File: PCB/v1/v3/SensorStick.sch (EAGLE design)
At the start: 56 parts, among them U1 TPD4F003DQDR, Y1 ECS-TXO-3225MV-400-TR

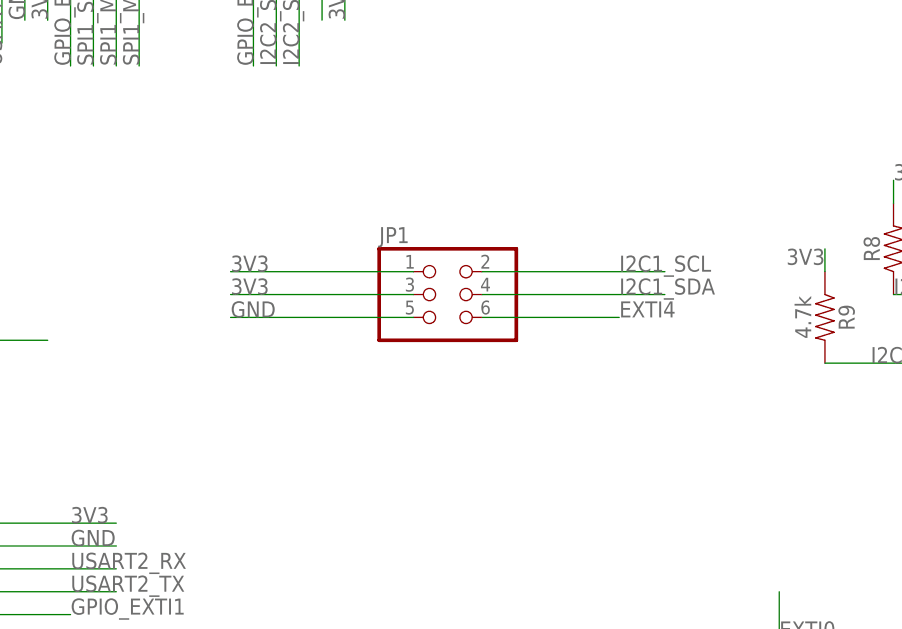
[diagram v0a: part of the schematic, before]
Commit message: Jesus - Rearranged to fit DIL24 socket for Mag breakout
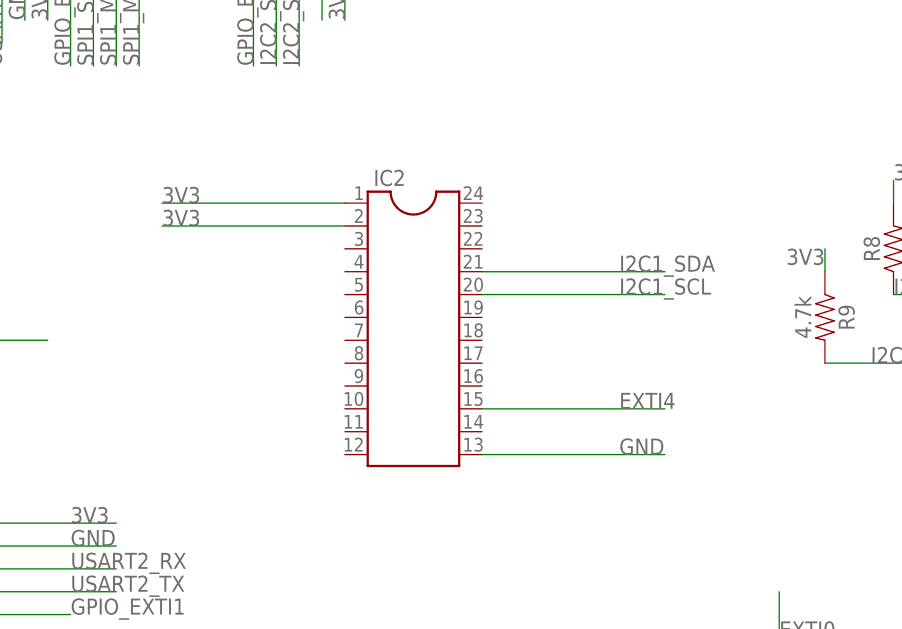
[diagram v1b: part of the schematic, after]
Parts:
- removed JP1: (no value), pinhead:PINHD-2X3
- added IC2: (no value), ic-package:DIL24-6
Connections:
- net 3V3: now also IC2.1, IC2.2; no longer JP1.1, JP1.3
- net EXTI4: now also IC2.15; no longer JP1.6
- net GND: now also IC2.13; no longer JP1.5
- net I2C1_SCL: now also IC2.20; no longer JP1.2
- net I2C1_SDA: now also IC2.21; no longer JP1.4
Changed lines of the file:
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@@
 <part name="U1" library="TPD4F003DQDR" deviceset="TPD4F003DQDR" device=""/>
 <part name="SV1" library="con-lsta" library_urn="urn:adsk.eagle:library:161" deviceset="FE05-1" device="" package3d_urn="urn:adsk.eagle:package:8190/1"/>
-<part name="JP1" library="pinhead" library_urn="urn:adsk.eagle:library:325" deviceset="PINHD-2X3" device="" package3d_urn="urn:adsk.eagle:package:22462/2"/>
 <part name="FRAME1" library="frames" library_urn="urn:adsk.eagle:library:229" deviceset="DINA3_L" device=""/>
+<part name="IC2" library="ic-package" library_urn="urn:adsk.eagle:library:239" deviceset="DIL24" device="-6" package3d_urn="urn:adsk.eagle:package:1009/2"/>
 </parts>
 <sheets>
@@
 <attribute name="NAME" x="102.87" y="97.282" size="1.778" layer="95"/>
 </instance>
-<instance part="JP1" gate="A" x="165.1" y="119.38" smashed="yes">
-<attribute name="NAME" x="158.75" y="125.095" size="1.778" layer="95"/>
-<attribute name="VALUE" x="158.75" y="111.76" size="1.778" layer="96"/>
-</instance>
 <instance part="FRAME1" gate="G$1" x="0" y="0" smashed="yes"/>
 <instance part="FRAME1" gate="G$2" x="287.02" y="0" smashed="yes">
@@
 <attribute name="SHEET" x="373.38" y="1.27" size="2.54" layer="94"/>
 <attribute name="DRAWING_NAME" x="304.8" y="19.05" size="2.54" layer="94"/>
+</instance>
+<instance part="IC2" gate="G$1" x="162.56" y="114.3" smashed="yes">
+<attribute name="NAME" x="158.115" y="131.445" size="1.778" layer="95"/>
+<attribute name="VALUE" x="158.115" y="97.79" size="1.778" layer="96"/>
 </instance>
 </instances>
@@
 </segment>
 <segment>
-<wire x1="162.56" y1="119.38" x2="142.24" y2="119.38" width="0.1524" layer="91"/>
-<label x="142.24" y="119.38" size="1.778" layer="95"/>
-<pinref part="JP1" gate="A" pin="3"/>
-</segment>
-<segment>
-<wire x1="162.56" y1="121.92" x2="142.24" y2="121.92" width="0.1524" layer="91"/>
-<pinref part="JP1" gate="A" pin="1"/>
-<label x="142.24" y="121.92" size="1.778" layer="95"/>
+<wire x1="154.94" y1="127" x2="134.62" y2="127" width="0.1524" layer="91"/>
+<label x="134.62" y="127" size="1.778" layer="95"/>
+<pinref part="IC2" gate="G$1" pin="2"/>
+</segment>
+<segment>
+<wire x1="154.94" y1="129.54" x2="134.62" y2="129.54" width="0.1524" layer="91"/>
+<label x="134.62" y="129.54" size="1.778" layer="95"/>
+<pinref part="IC2" gate="G$1" pin="1"/>
 </segment>
 </net>
@@
 </segment>
 <segment>
-<wire x1="162.56" y1="116.84" x2="142.24" y2="116.84" width="0.1524" layer="91"/>
-<label x="142.24" y="116.84" size="1.778" layer="95"/>
-<pinref part="JP1" gate="A" pin="5"/>
+<wire x1="170.18" y1="101.6" x2="190.5" y2="101.6" width="0.1524" layer="91"/>
+<label x="185.42" y="101.6" size="1.778" layer="95"/>
+<pinref part="IC2" gate="G$1" pin="13"/>
 </segment>
 </net>
@@
 </segment>
 <segment>
-<wire x1="190.5" y1="119.38" x2="170.18" y2="119.38" width="0.1524" layer="91"/>
-<label x="185.42" y="119.38" size="1.778" layer="95"/>
-<pinref part="JP1" gate="A" pin="4"/>
+<wire x1="190.5" y1="121.92" x2="170.18" y2="121.92" width="0.1524" layer="91"/>
+<label x="185.42" y="121.92" size="1.778" layer="95"/>
+<pinref part="IC2" gate="G$1" pin="21"/>
 </segment>
 </net>
@@
 </segment>
 <segment>
-<wire x1="190.5" y1="121.92" x2="170.18" y2="121.92" width="0.1524" layer="91"/>
-<label x="185.42" y="121.92" size="1.778" layer="95"/>
-<pinref part="JP1" gate="A" pin="2"/>
+<wire x1="190.5" y1="119.38" x2="170.18" y2="119.38" width="0.1524" layer="91"/>
+<label x="185.42" y="119.38" size="1.778" layer="95"/>
+<pinref part="IC2" gate="G$1" pin="20"/>
 </segment>
 </net>
@@
 </segment>
 <segment>
-<wire x1="170.18" y1="116.84" x2="185.42" y2="116.84" width="0.1524" layer="91"/>
-<label x="185.42" y="116.84" size="1.778" layer="95"/>
-<pinref part="JP1" gate="A" pin="6"/>
-</segment>
-</net>
+<wire x1="170.18" y1="106.68" x2="190.5" y2="106.68" width="0.1524" layer="91"/>
+<label x="185.42" y="106.68" size="1.778" layer="95"/>
+<pinref part="IC2" gate="G$1" pin="15"/>
+</segment>
+</net>
